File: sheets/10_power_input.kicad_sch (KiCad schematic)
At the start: 36 parts, among them J1 MSTB 2,5/5-GF-5,08, J2 MSTB 2,5/2-GF-5,08, Q101 STD18NF25, Q102 IPD30N10S3L-34, U101 LM74930QRGERQ1

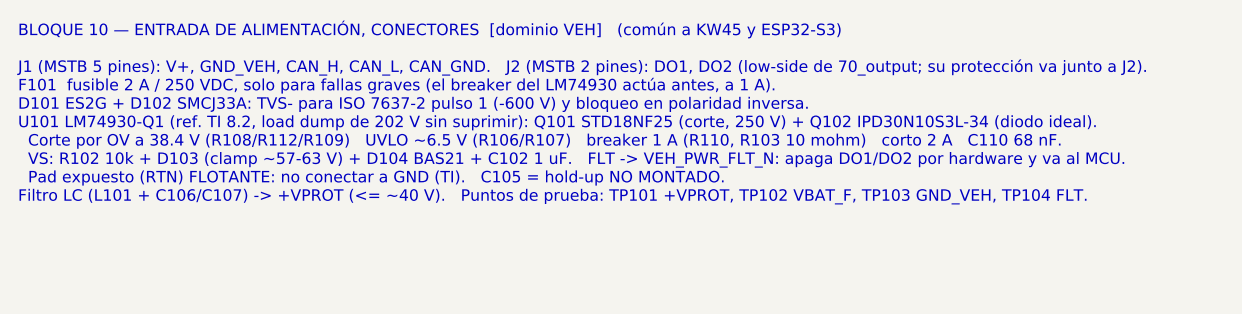
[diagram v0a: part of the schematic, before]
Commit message: Alcance: solo ESP32-S3, CAN clásico por TWAI, sin MCP2518FD
- Raíz: el bloque 40_mcu apunta a 40_mcu_esp32s3. 40_mcu_kw45 queda en
  el repo solo como referencia, fuera de la jerarquía.
- CAN: se eliminan el MCP2518FD, el cristal y los pines CANFD_SCK/MOSI/
  MISO, CS_CAN e INT_CAN en 60_can, 40_mcu_esp32s3 y la raíz (etiquetas,
  cables y pines de hoja). TWAI nativo (J1939) directo al ADM3055E.
  Se quita la variante CANFD.
- 20_isolation (nota): PS1 >= 5 W y entrada 9-72 V (corte OV 38.4 V);
  U2 = TPS7A1650-Q1 para +5V_VEH.
- 40_mcu_esp32s3 (nota): desacople 22 uF + 100 nF según Espressif y
  límite de 47 uF en +3V3_D por el TPS62A02-Q1; solo BLE en operación.
- README: tabla corregida (LM74930-Q1 en 10_power_input, 20, 30, 40, 60),
  sección MCU y "Requisitos para el firmware" (rearme del latch >= 100 ms,
  arranque limpio tras brownout, NimBLE con WiFi desactivado).
- CLAUDE.md: sección "Alcance" (ESP32-S3 único, dimensionar con WiFi).

ERC: 180 -> 160 violaciones; sin errores nuevos. Las restantes son de
hojas sin terminar (20, 30, 60) y etiquetas de la raíz sin destino.

Co-Authored-By: Claude Opus 5.5 <noreply@anthropic.com>
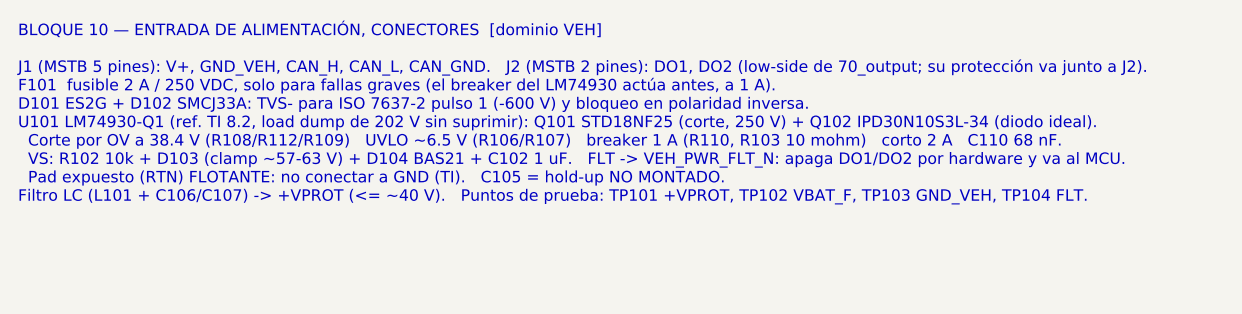
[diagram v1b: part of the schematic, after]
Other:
- note added: "BLOQUE 10 — ENTRADA DE ALIMENTACIÓN, CONECTORES [dominio VEH] J1 (MSTB 5 pines): V+, GND_VEH, CAN_H, CAN_L, CAN_GND. J2 (MSTB 2 pines): DO1, DO2 (low-side de 70_output; su protección va junto a J2). F101 fusible 2 A / 250 VDC, solo para fallas graves (el breaker del LM74930 actúa antes, a 1 A). D101 ES2G + D102 SMCJ33A: TVS- para ISO 7637-2 pulso 1 (-600 V) y bloqueo en polaridad inversa. U101 LM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"
- note removed: "BLOQUE 10 — ENTRADA DE ALIMENTACIÓN, CONECTORES [dominio VEH] (común a KW45 y ESP32-S3) J1 (MSTB 5 pines): V+, GND_VEH, CAN_H, CAN_L, CAN_GND. J2 (MSTB 2 pines): DO1, DO2 (low-side de 70_output; su protección va junto a J2). F101 fusible 2 A / 250 VDC, solo para fallas graves (el breaker del LM74930 actúa antes, a 1 A). D101 ES2G + D102 SMCJ33A: TVS- para ISO 7637-2 pulso 1 (-600 V) y bloqueo en 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"
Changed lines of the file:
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@@
 		(comment 2 "Inclinómetro de chasis CAN/BLE — INCLI-VA")
 	)
-	(text "BLOQUE 10 — ENTRADA DE ALIMENTACIÓN, CONECTORES  [dominio VEH]   (común a KW45 y ESP32-S3)\n\nJ1 (MSTB 5 pines): V+, GND_VEH, CAN_H, CAN_L, CAN_GND.   J2 (MSTB 2 pines): DO1, DO2 (low-side de 70_output; su protección va junto a J2).\nF101  fusible 2 A / 250 VDC, solo para fallas graves (el breaker del LM74930 actúa antes, a 1 A).\nD101 ES2G + D102 SMCJ33A: TVS- para ISO 7637-2 pulso 1 (-600 V) y bloqueo en polaridad inversa.\nU101 LM74930-Q1 (ref. TI 8.2, load dump de 202 V sin suprimir): Q101 STD18NF25 (corte, 250 V) + Q102 IPD30N10S3L-34 (diodo ideal).\n  Corte por OV a 38.4 V (R108/R112/R109)   UVLO ~6.5 V (R106/R107)   breaker 1 A (R110, R103 10 mohm)   corto 2 A   C110 68 nF.\n  VS: R102 10k + D103 (clamp ~57-63 V) + D104 BAS21 + C102 1 uF.   FLT -> VEH_PWR_FLT_N: apaga DO1/DO2 por hardware y va al MCU.\n  Pad expuesto (RTN) FLOTANTE: no conectar a GND (TI).   C105 = hold-up NO MONTADO.\nFiltro LC (L101 + C106/C107) -> +VPROT (<= ~40 V).   Puntos de prueba: TP101 +VPROT, TP102 VBAT_F, TP103 GND_VEH, TP104 FLT."
+	(text "BLOQUE 10 — ENTRADA DE ALIMENTACIÓN, CONECTORES  [dominio VEH]\n\nJ1 (MSTB 5 pines): V+, GND_VEH, CAN_H, CAN_L, CAN_GND.   J2 (MSTB 2 pines): DO1, DO2 (low-side de 70_output; su protección va junto a J2).\nF101  fusible 2 A / 250 VDC, solo para fallas graves (el breaker del LM74930 actúa antes, a 1 A).\nD101 ES2G + D102 SMCJ33A: TVS- para ISO 7637-2 pulso 1 (-600 V) y bloqueo en polaridad inversa.\nU101 LM74930-Q1 (ref. TI 8.2, load dump de 202 V sin suprimir): Q101 STD18NF25 (corte, 250 V) + Q102 IPD30N10S3L-34 (diodo ideal).\n  Corte por OV a 38.4 V (R108/R112/R109)   UVLO ~6.5 V (R106/R107)   breaker 1 A (R110, R103 10 mohm)   corto 2 A   C110 68 nF.\n  VS: R102 10k + D103 (clamp ~57-63 V) + D104 BAS21 + C102 1 uF.   FLT -> VEH_PWR_FLT_N: apaga DO1/DO2 por hardware y va al MCU.\n  Pad expuesto (RTN) FLOTANTE: no conectar a GND (TI).   C105 = hold-up NO MONTADO.\nFiltro LC (L101 + C106/C107) -> +VPROT (<= ~40 V).   Puntos de prueba: TP101 +VPROT, TP102 VBAT_F, TP103 GND_VEH, TP104 FLT."
 		(exclude_from_sim no)
 		(at 20.32 17.78 0)
